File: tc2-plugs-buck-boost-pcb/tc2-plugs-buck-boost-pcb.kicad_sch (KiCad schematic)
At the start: 61 parts, among them J1 JCON_M16_04Pin, J2 JCON_M16_2+4Pin, J3 Conn_02x06_Odd_Even, Q1 Q_PMOS_GSD, Q2 Q_PMOS_GSD, Q3 AO3400A, U201 TPS63070RNMR, U201 TPS63071

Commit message: v0.4.0
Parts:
- removed R9: 33k, Resistor_SMD:R_0603_1608Metric, symbol Device:R
- added D2: UESD3.3DT5G, Package_TO_SOT_SMD:SOT-723, symbol cacophony-library:UESD3.3DT5G
- added D3: MMBZ9V1ALT1G, Package_TO_SOT_SMD:SOT-23, symbol Diode:MMBZxx
- C205: LCSC (none) -> C15525
- C206, C207, C208, C209: LCSC C2980159 -> C86295
- C210: LCSC (none) -> C100072
- D1: LCSC C8062 -> C7497481
- FB1: LCSC C307778 -> C76818
- R10: value 22k -> 68k; footprint Resistor_SMD:R_0805_2012Metric -> Resistor_SMD:R_0402_1005Metric; LCSC C351592 -> C445618
- R201: LCSC C319588 -> C319591
- R7: value 560k -> 680k; footprint Resistor_SMD:R_1206_3216Metric -> Resistor_SMD:R_0805_2012Metric; LCSC C870794 -> C5151924
- R8: value 150k -> 100k; footprint Resistor_SMD:R_0805_2012Metric -> Resistor_SMD:R_0402_1005Metric; LCSC C136927 -> C445619
- U201: LCSC (none) -> C2876599
- U201: LCSC (none) -> C109322
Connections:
- net GND: now also R7.2, D2.3 (A), D3.3 (A)
- net OUT_RX: now also D2.1 (K)
- net OUT_TX: now also D2.2 (K)
- net SPEAKER_+: now also D3.1 (K)
- net SPEAKER_-: now also D3.2 (K)

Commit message: Small update for v0.4.1
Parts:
- R5, R6: footprint Resistor_SMD:R_1210_3225Metric -> Resistor_SMD:R_0805_2012Metric; LCSC C304148 -> C2984387
- R7: footprint Resistor_SMD:R_0805_2012Metric -> Resistor_SMD:R_0603_1608Metric; LCSC C5151924 -> C326722
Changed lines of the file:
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@@
 			)
 		)
-		(property "Footprint" "Resistor_SMD:R_1210_3225Metric"
+		(property "Footprint" "Resistor_SMD:R_0805_2012Metric"
 			(at 31.242 40.64 90)
 			(effects
@@
 			)
 		)
-		(property "LCSC" "C304148"
+		(property "LCSC" "C2984387"
 			(at 33.02 40.64 0)
 			(effects
@@
 			)
 		)
-		(property "Footprint" "Resistor_SMD:R_0805_2012Metric"
+		(property "Footprint" "Resistor_SMD:R_0603_1608Metric"
 			(at 31.242 50.8 90)
 			(effects
@@
 			)
 		)
-		(property "LCSC" "C5151924"
+		(property "LCSC" "C326722"
 			(at 33.02 50.8 0)
 			(effects
@@
 			)
 		)
-		(property "Footprint" "Resistor_SMD:R_1210_3225Metric"
+		(property "Footprint" "Resistor_SMD:R_0805_2012Metric"
 			(at 52.832 40.64 90)
 			(effects
@@
 			)
 		)
-		(property "LCSC" "C304148"
+		(property "LCSC" "C2984387"
 			(at 54.61 40.64 0)
 			(effects

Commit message: Adding panel
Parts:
- removed D2: UESD3.3DT5G, Package_TO_SOT_SMD:SOT-723, symbol cacophony-library:UESD3.3DT5G
- removed D3: MMBZ9V1ALT1G, Package_TO_SOT_SMD:SOT-23, symbol Diode:MMBZxx
- added D5: SMF05CT1G, cacophony-library:SOT-363_L2.0-W1.3-P0.65-LS2.1-BR, symbol cacophony-library:SMF05CT1G
- added R9: 100k, Resistor_SMD:R_0402_1005Metric, symbol Device:R
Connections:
- net +3V3: now also R9.1
- net 5V_EN: now also R9.2
- net GND: now also D5.2
- net OUT_RX: now also D5.6
- net OUT_TX: now also D5.1
- net SPEAKER_+: now also D5.4
- net SPEAKER_-: now also D5.5
- no-connect marks 3 -> 4

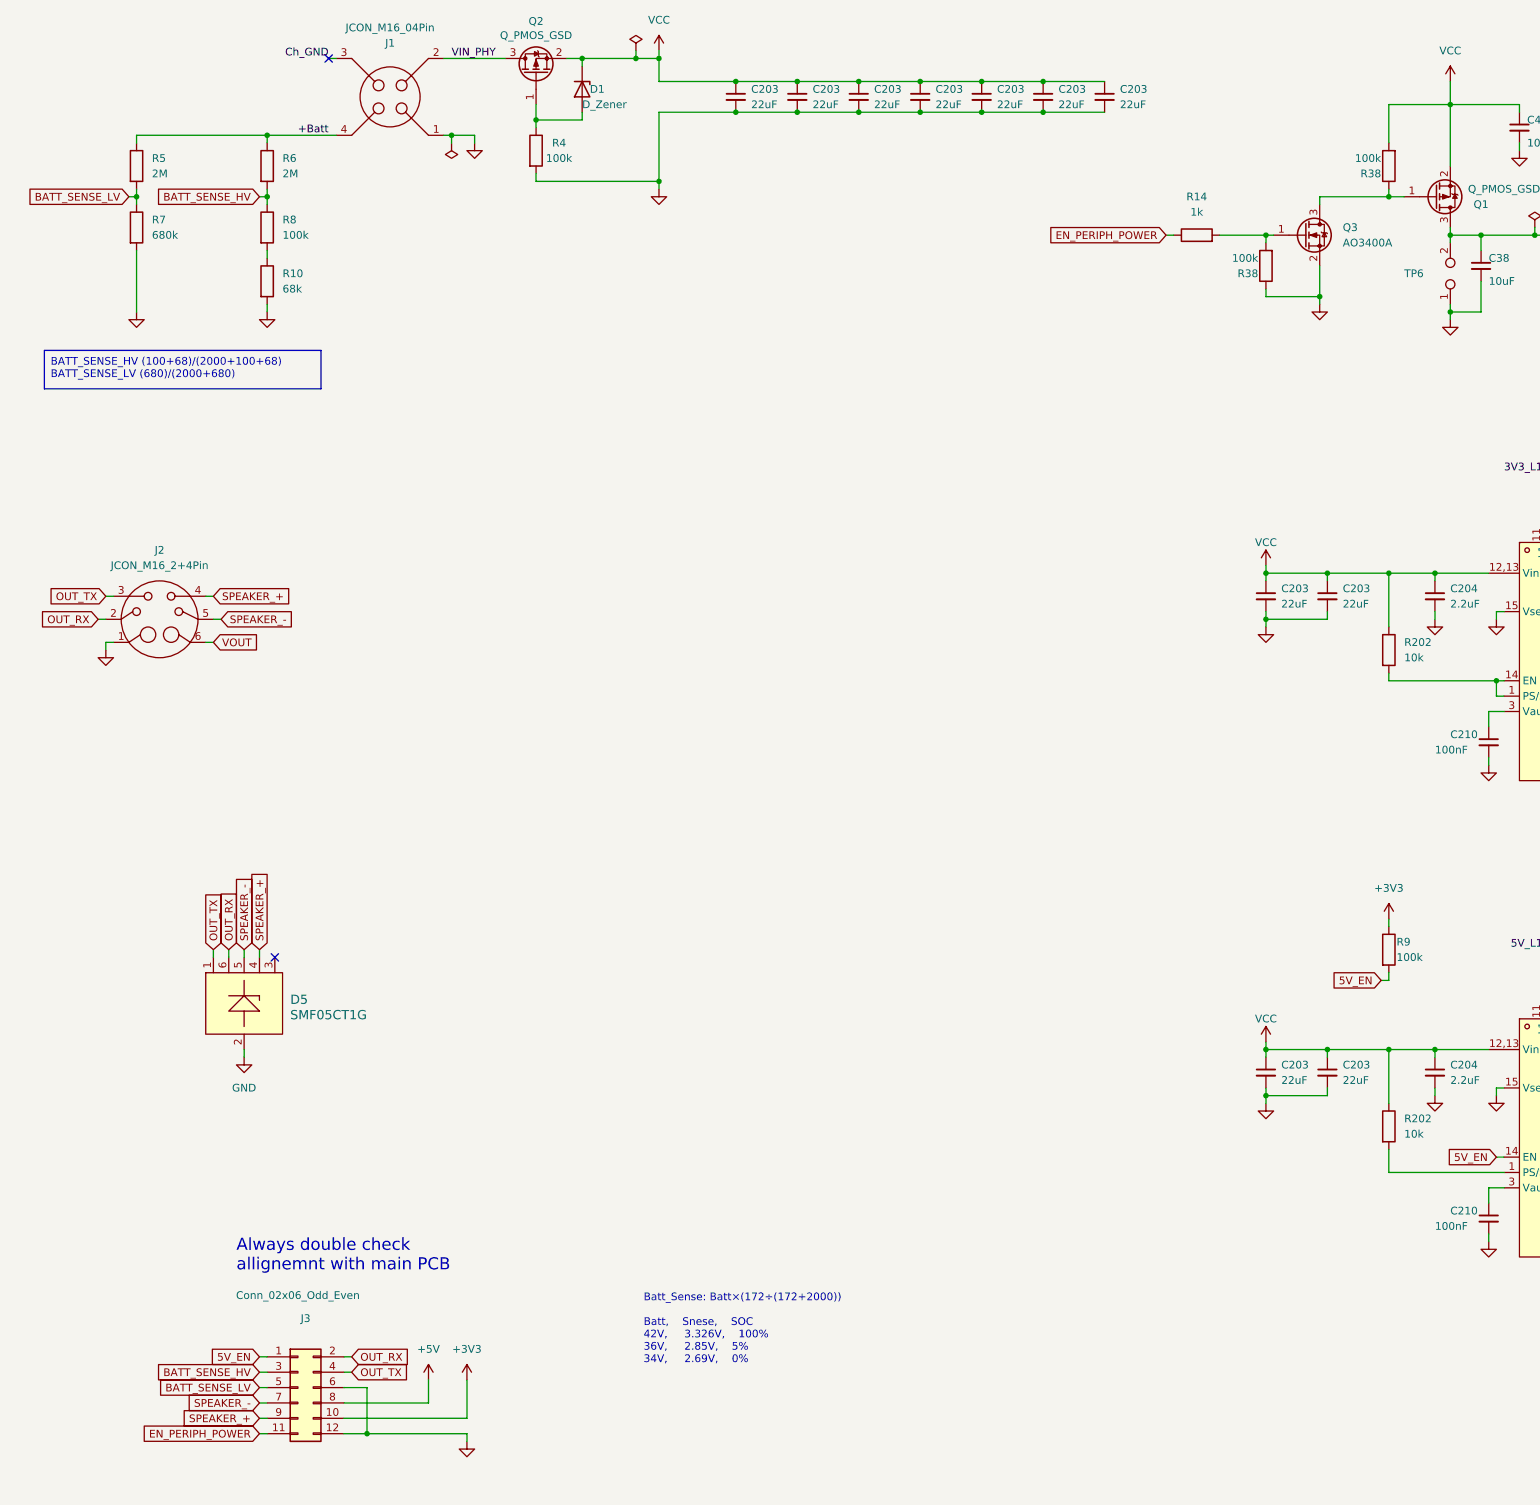
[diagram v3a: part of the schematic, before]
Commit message: Update to use touch sensor
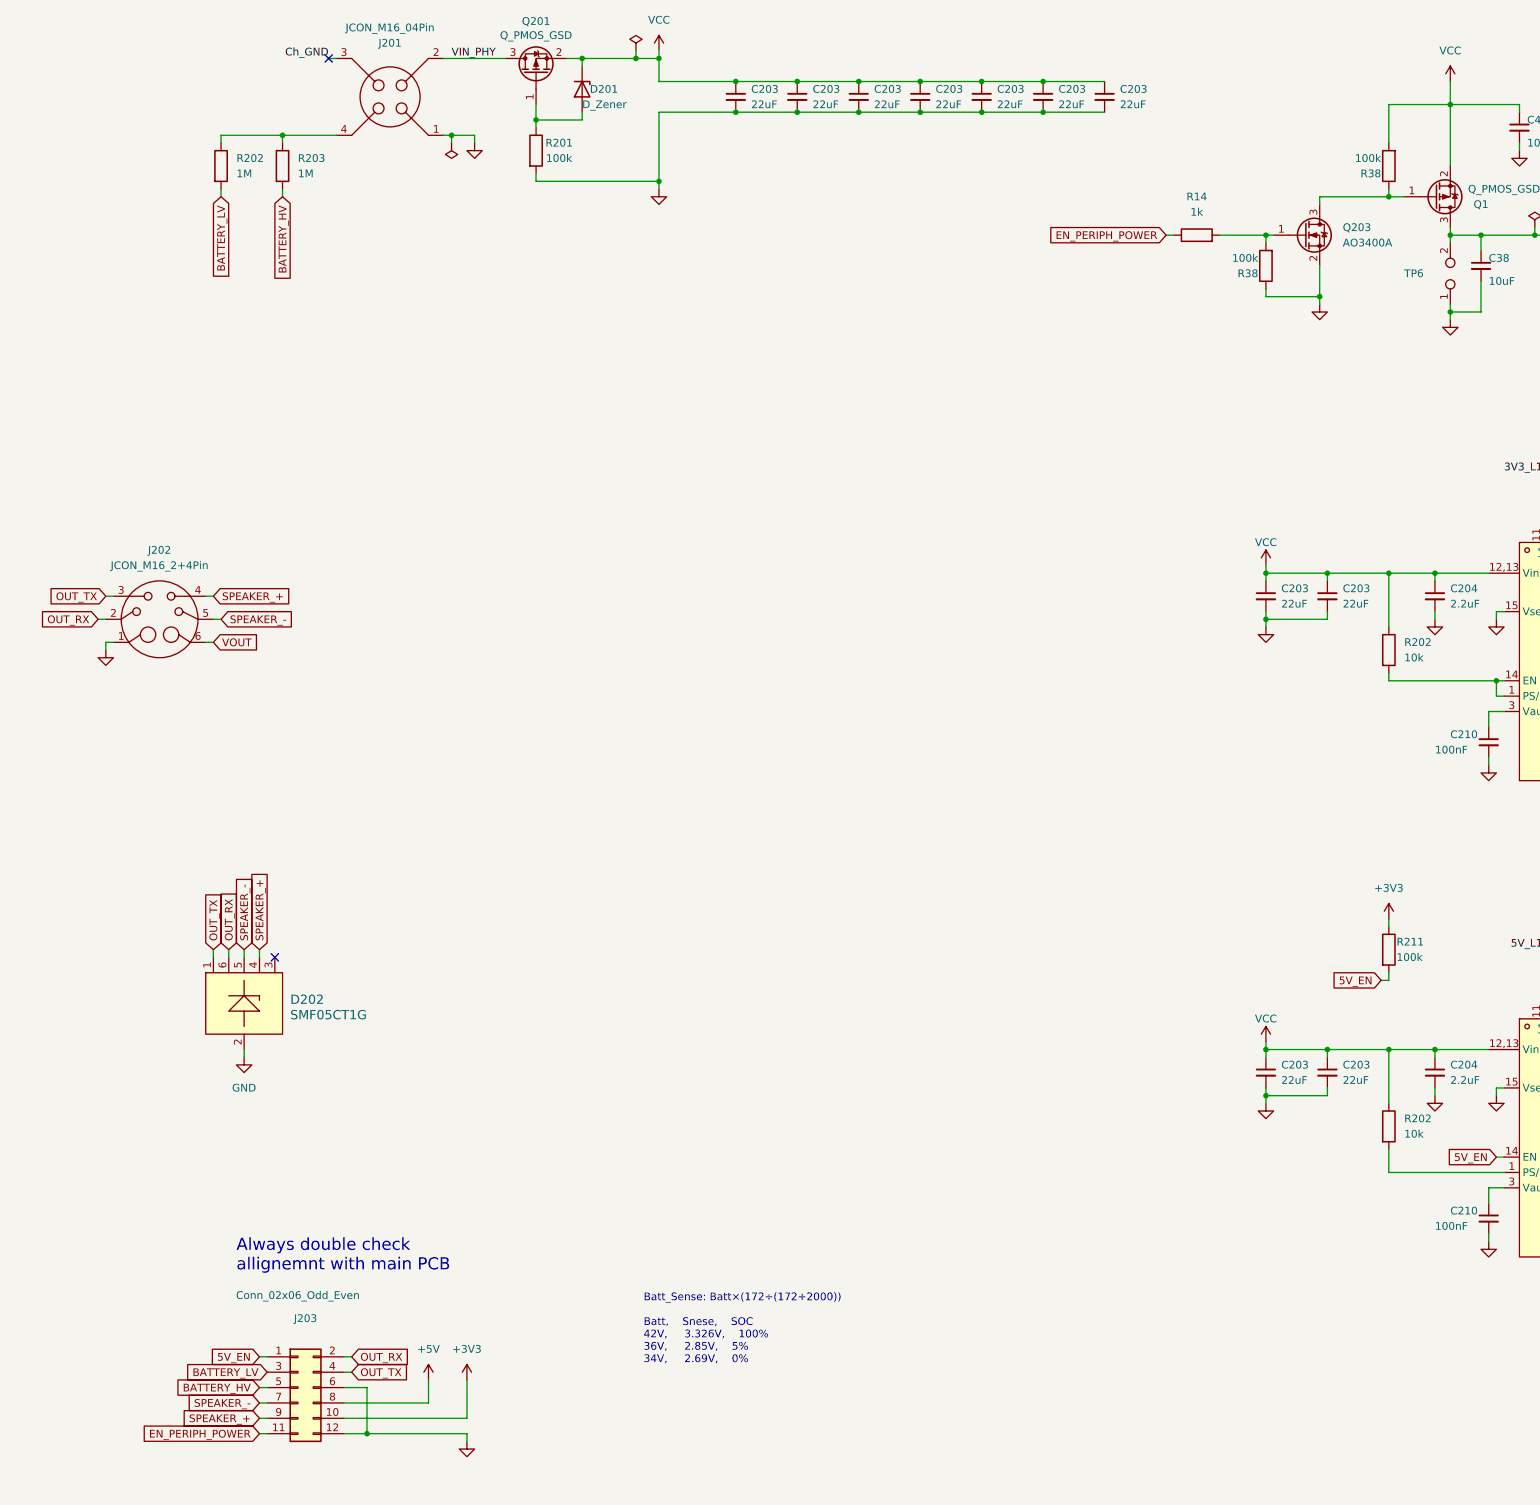
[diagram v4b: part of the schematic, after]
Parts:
- removed R10: 68k, Resistor_SMD:R_0402_1005Metric, symbol Device:R
- removed R5, R6: 2M, Resistor_SMD:R_0805_2012Metric, symbol Device:R
- removed R7: 680k, Resistor_SMD:R_0603_1608Metric, symbol Device:R
- removed R8: 100k, Resistor_SMD:R_0402_1005Metric, symbol Device:R
- added R202, R203: 1M, Resistor_SMD:R_0603_1608Metric, symbol Device:R
- L3: LCSC C2042459 -> C5179452
- renumbered D1 to D201, D5 to D202, J1 to J201, J2 to J202, J3 to J203, Q2 to Q201, Q3 to Q203, R4 to R201, R9 to R211
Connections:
- net +Batt: no longer names the net of J201.4
- net +Batt: now also R202.1, R203.1
- net BATT_SENSE_HV renamed BATTERY_LV
- net BATTERY_LV: now also R202.2
- net BATT_SENSE_LV renamed BATTERY_HV
- net BATTERY_HV: now also R203.2

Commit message: Small updates
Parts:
- added C228: 1uF, Capacitor_SMD:C_1206_3216Metric, symbol Device:C_Small
- added R217: 180R, Resistor_SMD:R_0402_1005Metric, symbol Device:R
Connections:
- net GND: now also C228.2
- net at R202.1, R203.1: now also C228.1, R217.1; no longer J201.4
- new net: J201.4, R217.2
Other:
- moved on the sheet: R202, R203

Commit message: v0.7.2 panelise microphone boards
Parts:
- removed J203: Conn_02x06_Odd_Even, cacophony-library:PinHeader_2x06_P2.00mm_Horizontal, symbol Connector_Generic:Conn_02x06_Odd_Even
- removed R201: 680k, Resistor_SMD:R_0402_1005Metric, symbol Device:R
- removed R202: 10k, Resistor_SMD:R_0402_1005Metric, symbol Device:R
- removed R203: 130k, Resistor_SMD:R_0402_1005Metric, symbol Device:R
- added F201: 2A, Fuse:Fuse_0603_1608Metric, symbol Device:Fuse
- added F202: Fuse, symbol Device:Fuse
- added J204: Conn_02x07_Odd_Even, symbol Connector_Generic:Conn_02x07_Odd_Even
- added R213, R219: 100k, Resistor_SMD:R_0402_1005Metric, symbol Device:R
- added R216: 470k, Resistor_SMD:R_0402_1005Metric, symbol Device:R
- added R218: 68k, Resistor_SMD:R_0402_1005Metric, symbol Device:R
- added U203, U207, U208, U209: ICSRC3908SFR, cacophony-library:CONN-SMD_L3.9-W0.8, symbol cacophony-library:ICSRC3908SFR
- L3: value INDUCTOR -> 1.5uH
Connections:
- net +3V3: now also J204.10 (Pin_10), R213.1
- net +5V: now also J204.8 (Pin_8)
- net 5V_EN: now also J204.1 (Pin_1)
- net 5V_PHY: now also R216.1; no longer U201.5 (FB)
- net BATTERY_HV: now also J204.5 (Pin_5)
- net BATTERY_LV: now also J204.3 (Pin_3)
- net EN_PERIPH_POWER: now also J204.11 (Pin_11)
- net GND: now also J204.12 (Pin_12), J204.6 (Pin_6), R219.2, U203.1, U207.1, U208.1, U209.1
- net OUT_RX: now also J204.2 (Pin_2)
- net OUT_TX: now also J204.4 (Pin_4)
- net SPEAKER_+: now also J204.9 (Pin_9)
- net SPEAKER_-: now also J204.7 (Pin_7)
- net VIN_PHY: now also F202.1; no longer Q201.3 (D)
- net VOUT: now also F201.2; no longer C38.1, Q1.3 (D), TP6.2
- net 3V3_FB: now reaches R201.2, R203.1, U201.5 (FB)
- net BATT: now reaches C228.1, R202.1, R203.1, R217.1
- net POWER_SAVE_EN: now reaches U201.1 (PS/SYNC)
- net POWER_SAVE_EN: now also U201.1 (PS/SYNC), J204.13 (Pin_13), R213.2
- net 5V_PG: now reaches R38.2, U201.2 (PG)
- net 3V3_PG: now reaches R38.2, U201.2 (PG)
- net at R202.2, U201.14 (EN): no longer U201.1 (PS/SYNC)
- net BATT_PHY: now reaches J201.4, R217.2
- new net: C38.1, F201.1, Q1.3 (D), TP6.2
- new net: F202.2, Q201.3 (D)
- new net: R218.1, R219.1, U201.5 (FB)
- new net: R216.2, R218.2
- no-connect marks 4 -> 3
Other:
- note added: "C187606"
- note removed: "- C239344, C92271: female, 2.54 - C239355: angled, female, 2.54, - C239335: angled, male, 2.54 - BF060-08A-B-0600-0280-0305-L-D: angled, male, 2mm, 6mm mating length"
- note removed: "Batt_Sense: Batt×(172÷(172+2000)) Batt, Snese, SOC 42V, 3.326V, 100% 36V, 2.85V, 5% 34V, 2.69V, 0%"
- moved on the sheet: C203, C38, C43, D201, Q1, Q201, Q203, R14, R201, R38, TP6

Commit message: v0.7.3
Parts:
- removed C203 (x2): 22uF, Capacitor_SMD:C_0805_2012Metric, symbol Device:C_Small
- removed C204: 2.2uF, Capacitor_SMD:C_0402_1005Metric, symbol Device:C_Small
- removed C205: 10uF, Capacitor_SMD:C_0402_1005Metric, symbol Device:C_Small
- removed C206, C207, C208, C209: 22uF, Capacitor_SMD:C_0603_1608Metric, symbol Device:C_Small
- removed D201: D_Zener, cacophony-library:LL-34_L3.5-W1.5-RD, symbol Device:D_Zener
- removed F202: Fuse, symbol Device:Fuse
- removed FB1: FerriteBead, Inductor_SMD:L_0805_2012Metric, symbol Device:FerriteBead
- removed L3: 1.5uH, Inductor_SMD:L_1008_2520Metric, symbol cacophony-library:Power_Inductor
- removed Q201: Q_PMOS_GSD, Package_TO_SOT_SMD:SOT-23, symbol Device:Q_PMOS_GSD
- removed R201, R38: 100k, Resistor_SMD:R_0402_1005Metric, symbol Device:R
- removed R201: 470k, Resistor_SMD:R_0402_1005Metric, symbol Device:R
- removed R202: 10k, Resistor_SMD:R_0402_1005Metric, symbol Device:R
- removed R203: 150k, Resistor_SMD:R_0402_1005Metric, symbol Device:R
- removed U201: TPS63070RNMR, cacophony-library:TPS63070, symbol cacophony-library:TPS63070RNMR
- removed U203, U207, U208, U209: ICSRC3908SFR, cacophony-library:CONN-SMD_L3.9-W0.8, symbol cacophony-library:ICSRC3908SFR
- added C1001, C1002: 22uF, Capacitor_SMD:C_0805_2012Metric, symbol Device:C_Small
- added C1003: 2.2uF, Capacitor_SMD:C_0402_1005Metric, symbol Device:C_Small
- added C1004: 10uF, Capacitor_SMD:C_0402_1005Metric, symbol Device:C_Small
- added C1005, C1006, C1007, C1008: 22uF, Capacitor_SMD:C_0603_1608Metric, symbol Device:C_Small
- added C1009: 100nF, Capacitor_SMD:C_0402_1005Metric, symbol Device:C_Small
- added FB1001: FerriteBead, Inductor_SMD:L_0805_2012Metric, symbol Device:FerriteBead
- added L1001: 1.5uH, Inductor_SMD:L_1008_2520Metric, symbol cacophony-library:Power_Inductor
- added R1004: 100k, Resistor_SMD:R_0402_1005Metric, symbol Device:R
- added R201: 680Ω, Resistor_SMD:R_0402_1005Metric, symbol Device:R
- added R221: 470k, Resistor_SMD:R_0402_1005Metric, symbol Device:R
- added R222: 150k, Resistor_SMD:R_0402_1005Metric, symbol Device:R
- added TP204: TestPoint, cacophony-library:TP_PAD, symbol Connector:TestPoint
- added U1001, U1002, U1003, U1004, U206, U210, U211, U212: ICSRC3908SFR, cacophony-library:CONN-SMD_L3.9-W0.8, symbol cacophony-library:ICSRC3908SFR
- added U1005: TPS63070, cacophony-library:TPS63070, symbol cacophony-library:TPS63070RNMR
- added U203: TPS259541DSGR, cacophony-library:WFDFN-8_L2.0-W2.0-P0.50-BL-EP, symbol cacophony-library:TPS259541DSGR
- C210: value 100nF -> 8.2nF; LCSC C100072 -> C309459
- J204: footprint (none) -> cacophony-library:PinHeader_2x07_P2.00mm_Horizontal; now not fitted
- U201: value TPS63071 -> TPS63070; symbol cacophony-library:TPS63071 -> cacophony-library:TPS63070RNMR; LCSC C2876599 -> C109322; LCSC Part C2876599 -> C109322
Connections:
- net +3V3: now also FB1001.2
- net 3V3_L1: now also L1001.1, U1005.11 (L1)
- net 3V3_L2: now also L1001.2, U1005.9 (L2)
- net 3V3_PG: now also R1004.2, U1005.2 (PG)
- net 3V3_PHY: now also C1004.1, C1005.1, C1006.1, C1007.1, C1008.1, FB1001.1, R1004.1, R221.1, U1005.7,8 (Vout)
- net BATTERY_HV: now also J204.3 (Pin_3); no longer J204.5 (Pin_5)
- net BATTERY_LV: now also J204.5 (Pin_5); no longer J204.3 (Pin_3)
- net GND: now also C1001.2, C1002.2, C1003.2, C1004.2, C1005.2, C1006.2, C1007.2, C1008.2, C1009.2, R201.2, R222.2, U1001.1, U1002.1, U1003.1, U1004.1, U1005.10 (PGND), U1005.15 (Vsel), U1005.4 (GND), U1005.6 (FB2), U203.8 (GND), U203.9 (GND), U206.1, U210.1, U211.1, U212.1
- net SPEAKER_+: now also D202.5, J204.7 (Pin_7); no longer D202.4, J204.9 (Pin_9)
- net SPEAKER_-: now also D202.4, J204.9 (Pin_9); no longer D202.5, J204.7 (Pin_7)
- net VCC: now also C1001.1, C1002.1, C1003.1, U1005.12,13 (Vin), U1005.14 (EN), U203.5 (OUT)
- net VIN_PHY: now also U203.2 (EN/UVLO), U203.3 (IN), U203.4 (IN)
- net Vout_PHY: now reaches C38.1, F201.1, Q1.3 (D), TP6.2
- net at C210.1: now also U203.1 (dVdt)
- net POWER_SAVE_EN renamed BUCK_BOOST_FPWM
- net BUCK_BOOST_FPWM: now also U1005.1 (PS/SYNC)
- new net: R221.2, R222.1, U1005.5 (FB)
- new net: C1009.1, U1005.3 (Vaux)
- new net: R201.1, U203.7 (ILM)
- new net: TP204.1, U203.6 (~{FLT})
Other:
- note added: "TPS259541DSG"
- note removed: "C187606"
- moved on the sheet: C203, C204, C205, C206, C207, C208, C209, C210, FB1, L3, R211, R213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

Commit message: New power changes WIP
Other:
- note added: "TPS25947xx"
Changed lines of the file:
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@@
+		)
+	)
+	(text_box "CMC\nC41519\nC78245"
+		(exclude_from_sim no)
+		(at 95.25 158.75 0)
+		(size 27.94 13.97)
+		(stroke
+			(width 0)
+			(type default)
+		)
+		(fill
+			(type none)
+		)
+		(effects
+			(font
+				(size 1.27 1.27)
+			)
+			(justify left top)
 		)
 	)
@@
 		)
 	)
+	(text "TPS25947xx"
+		(exclude_from_sim no)
+		(at 128.27 13.462 0)
+		(effects
+			(font
+				(size 1.27 1.27)
+			)
+		)
+	)
 	(label "3V3_PG"
 		(at 287.02 168.91 0)
@@
 				(hide yes)
 			)
+		)
+	)
+	(global_label "CMC TODO"
+		(shape input)
+		(at 95.25 154.94 0)
+		(fields_autoplaced yes)
+		(effects
+			(font
+				(size 1.27 1.27)
+			)
+			(justify left)
+		)
+		(property "Intersheetrefs" "${INTERSHEET_REFS}"
+			(at 108.0928 154.94 0)
+			(effects
+				(font
+					(size 1.27 1.27)
+				)
+				(justify left)
+				(hide yes)
+			)
